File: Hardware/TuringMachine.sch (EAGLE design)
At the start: 91 parts, among them IC1 TL072P, IC11 78L09, IC12 78L09, IC5 4016, IC6 TL072P, IC7 TL072P, T1 2N3904

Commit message: add 100k resistor after noise comparator
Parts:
- removed IC5: 4016, 40xx:4016N
- added BACK_BUS: (no value), MusicThingModular:MA07-2_BACKSIDEFRONTSIDE
- added BACK_PWR: (no value), con-lstb:MA03-2
- added FRONT_BUS: (no value), MusicThingModular:MA07-2_BACKSIDEBACKSIDE
- added FRONT_PWR: (no value), MusicThingModular:MA03-2BACKSIDE
- added R4: 100k, TomW:R-EU_0207/7
- added SWITCH_IC: 4016, 40xx:4016N
- CLOCK, CV_IN, CV_OUT, NOISE-OUT: value THONKICONN -> THONKICONNNEW; device MusicThingModular:THONKICONN -> MusicThingModular:THONKICONNNEW
- R11: device MusicThingModular:RESISTOR6MM -> MusicThingModular:RESISTOR7MM
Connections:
- net NOISE renamed NOISE_FRONT
- removed net -12V: R35.1
- removed net B1: 1.A, LENGTH.6, R14.2, SHIFTREG_MAINA.QD, U$2.B1-MSB
- removed net B2: 2.A, SHIFTREG_MAINA.QC, U$2.B2
- removed net B3: 3.A, LENGTH.5, SHIFTREG_MAINA.QB, U$2.B3
- removed net B4: 4.A, LENGTH.4, SHIFTREG_MAINA.QA, U$2.B4
- removed net B5: 5.A, LENGTH.3, R8.1, SHIFTREG_MAINB.QD, U$2.B5
- removed net B6: 6.A, LENGTH.2, SHIFTREG_MAINB.QC, U$2.B6
- removed net B7: 7.A, LENGTH.1, SHIFTREG_MAINB.QB, U$2.B7
- removed net B8: 8.A, SHIFTREG_MAINB.QA, U$2.B8-LSB
- removed net BIT1_BACK: AND_2D.I0, BUFFER2F.I
- removed net BIT2_BACK: AND_2C.I1, BUFFER2E.I
- removed net BIT3_BACK: AND_2A.I0, BUFFER2A.I
- removed net BIT4_BACK: AND_2B.I0, BUFFER2B.I
- removed net BIT5_BACK: AND_1D.I0, BUFFER1E.I
- removed net BIT6_BACK: AND_1C.I0, BUFFER1D.I
- removed net BIT7_BACK: AND_1B.I0, BUFFER1C.I
- removed net BIT8_BACK: AND_1A.I0, BUFFER1A.I
- removed net CLOCKIN: CLK.A, D2.C, R12.2, R7.2, SHIFTREG_EXTA.CLK, SHIFTREG_EXTB.CLK, SHIFTREG_MAINA.CLK, SHIFTREG_MAINB.CLK
- removed net END_OF_LOOP: IC5A.A, IC5C.C, LENGTH.A
- removed net GND: C1.1, C2.2, C3.1, C4.1, CV_IN.5, IC5C.B, IC5D.B, IC6A.+IN, SHIFTREG_EXTA.RES, SHIFTREG_EXTB.RES, SHIFTREG_MAINA.RES, SHIFTREG_MAINB.RES, VR2.P$1, WRITE.S
- removed net N$24: IC5A.C, IC5D.C, IC6B.OUT
- removed net STEP_12: C3.2, LENGTH.7, R15.2, SHIFTREG_EXTA.D
- removed net STEP_16: LENGTH.8, SHIFTREG_EXTA.QD
- new net B1_BACK: AND_2D.I0, BACK_BUS.1, BUFFER2F.I, R14.2, SHIFTREG_MAINA.QD
- new net B1_FRONT: 1.A, FRONT_BUS.1, LENGTH.6, U$2.B1-MSB
- new net B2_BACK: AND_2C.I1, BACK_BUS.2, BUFFER2E.I, SHIFTREG_MAINA.QC
- new net B2_FRONT: 2.A, FRONT_BUS.2, U$2.B2
- new net B3_BACK: AND_2A.I0, BACK_BUS.3, BUFFER2A.I, SHIFTREG_MAINA.QB
- new net B3_FRONT: 3.A, FRONT_BUS.3, LENGTH.5, U$2.B3
- new net B4_BACK: AND_2B.I0, BACK_BUS.4, BUFFER2B.I, SHIFTREG_MAINA.QA
- new net B4_FRONT: 4.A, FRONT_BUS.4, LENGTH.4, U$2.B4
- new net B5_BACK: AND_1D.I0, BACK_BUS.5, BUFFER1E.I, R8.1, SHIFTREG_MAINB.QD
- new net B5_FRONT: 5.A, FRONT_BUS.5, LENGTH.3, U$2.B5
- new net B6_BACK: AND_1C.I0, BACK_BUS.6, BUFFER1D.I, SHIFTREG_MAINB.QC
- new net B6_FRONT: 6.A, FRONT_BUS.6, LENGTH.2, U$2.B6
- new net B7_BACK: AND_1B.I0, BACK_BUS.7, BUFFER1C.I, SHIFTREG_MAINB.QB
- new net B7_FRONT: 7.A, FRONT_BUS.7, LENGTH.1, U$2.B7
- new net B8_BACK: AND_1A.I0, BACK_BUS.8, BUFFER1A.I, SHIFTREG_MAINB.QA
- new net B8_FRONT: 8.A, FRONT_BUS.8, U$2.B8-LSB
- new net CLOCK_FRONT: CLK.A, D2.C, FRONT_BUS.11, R12.2, R7.2
- new net END_OF_LOOP_BACK: BACK_BUS.14, SWITCH_ICA.A, SWITCH_ICC.C
- new net END_OF_LOOP_FRONT: FRONT_BUS.14, LENGTH.A
- new net LOOP_CTRL_BACK: BACK_BUS.12, SWITCH_ICA.C, SWITCH_ICD.C
- new net LOOP_CTRL_FRONT: FRONT_BUS.12, R4.2
- new net N$1: IC6B.OUT, R4.1
- new net STEP_12_BACK: BACK_BUS.9, C3.2, R15.2, SHIFTREG_EXTA.D
- new net STEP_12_FRONT: FRONT_BUS.9, LENGTH.7
- new net STEP_16_BACK: BACK_BUS.10, SHIFTREG_EXTA.QD
- new net STEP_16_FRONT: FRONT_BUS.10, LENGTH.8
- new net WRITE_SW_FRONT: FRONT_BUS.13, R18.2
- net +12V_BACK: now also BACK_PWR.5, BACK_PWR.6, L1.2, R1.2, R24.2, SHIFTREG_EXTP.VDD, SHIFTREG_MAINP.VDD, SWITCH_ICP.VDD; no longer L1.1
- net +12V_FRONT: now also FRONT_PWR.5, FRONT_PWR.6; no longer IC5P.VDD, R1.2, R24.2, SHIFTREG_EXTP.VDD, SHIFTREG_MAINP.VDD
- net -12V_BACK: now also BACK_PWR.1, BACK_PWR.2, L2.2; no longer L2.1
- net -12V_FRONT: now also FRONT_PWR.1, FRONT_PWR.2, R35.1
- net CLOCK_BACK: now also BACK_BUS.11, SHIFTREG_EXTA.CLK, SHIFTREG_EXTB.CLK, SHIFTREG_MAINA.CLK, SHIFTREG_MAINB.CLK
- net GND_BACK: now also BACK_PWR.3, BACK_PWR.4, C1.1, C2.2, C3.1, C4.1, SHIFTREG_EXTA.RES, SHIFTREG_EXTB.RES, SHIFTREG_EXTP.VSS, SHIFTREG_MAINA.RES, SHIFTREG_MAINB.RES, SHIFTREG_MAINP.VSS, SWITCH_ICC.B, SWITCH_ICD.B, SWITCH_ICP.VSS
- net GND_FRONT: now also CV_IN.5, FRONT_PWR.3, FRONT_PWR.4, IC6A.+IN, VR2.P$1, WRITE.S; no longer IC5P.VSS, SHIFTREG_EXTP.VSS, SHIFTREG_MAINP.VSS
- net N$4: now also SWITCH_ICB.A, SWITCH_ICC.A; no longer IC5B.A, IC5C.A
- net N$42: now also L1.1; no longer L1.2
- net N$44: now also L2.1; no longer L2.2
- net N$45: now also SWITCH_ICB.C, SWITCH_ICD.A; no longer IC5B.C, IC5D.A
- net START_OF_LOOP: now also BACK_BUS.13, SWITCH_ICA.B, SWITCH_ICB.B; no longer IC5A.B, IC5B.B, R18.2
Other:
- note added: "Channels between front and back: GND +12V -12V STEP_16_FRONT - STEP_16_BACK STEP_12_FRONT - STEP_12_BACK CLOCK_FRONT - CLOCK_BACK END_OF_LOOP_FRONT - END_OF_LOOP_BACKRL LOOP_CTRL_FRONT - LOOP_CTRL_BACK WRITE_SW_FRONT - START_OF_LOOP B1(-B8)_FRONT - B1(-B8)_BACK"
- moved on the sheet: AND_1A, AND_1B, AND_1C, AND_1D, AND_2A, AND_2B, AND_2C, AND_2D, BUFFER1A, BUFFER1B, BUFFER1C, BUFFER1D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

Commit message: routing
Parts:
- removed IC1, IC6: TL072P, TomW:TL072P
- added U1: TL074_, MusicThingModular:TL074_
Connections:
- net N$29 renamed +9V_1
- net N$38 renamed +9V_2
- new net N$17: R16.2, SWITCH_ICA.B, SWITCH_ICB.B
- net +12V_FRONT: now also R29.2, U1P.V+; no longer IC1P.V+, IC6P.V+, R29.1
- net -12V_FRONT: now also U1P.V-; no longer IC1P.V-, IC6P.V-
- net B1_BACK: now also AND_2C.I0, BUFFER2D.I, R14.1; no longer AND_2D.I0, BUFFER2F.I, R14.2
- net B2_BACK: now also AND_2D.I1; no longer AND_2C.I1
- net B3_BACK: now also AND_2B.I0, BUFFER2C.I; no longer AND_2A.I0, BUFFER2A.I
- net B4_BACK: now also AND_2A.I0; no longer AND_2B.I0
- net B8_BACK: now also BUFFER1B.I; no longer BUFFER1A.I
- net BUFFCLK2_BACK: now also BUFFER1A.O; no longer BUFFER2D.O
- net BUFFCLK_BACK: now also AND_2C.I1, AND_2D.I0, BUFFER2A.O; no longer AND_2C.I0, AND_2D.I1, BUFFER2C.O
- net CLOCK_BACK: now also BUFFER1A.I, BUFFER2A.I; no longer BUFFER2C.I, BUFFER2D.I
- net CLOCK_FRONT: now also R13.2; no longer CLK.A
- net GATE1: now also BUFFER2D.O; no longer BUFFER2F.O
- net GATE3: now also BUFFER2C.O; no longer BUFFER2A.O
- net GATE8: now also BUFFER1B.O; no longer BUFFER1A.O
- net GND_BACK: now also BUFFER2F.I, C2.1; no longer BUFFER1B.I, C2.2
- net GND_FRONT: now also CLK.C, U1A.+IN, U1B.+IN, U1C.+IN; no longer IC1A.+IN, IC1B.+IN, IC6A.+IN, R13.1
- net N$1: now also U1D.OUT; no longer IC6B.OUT
- net N$15: now also CLK.A, R13.1; no longer CLK.C, R13.2
- net N$16: now also R29.1; no longer R29.2
- net N$21: now also U1A.-IN; no longer IC1A.-IN
- net N$22: now also U1A.OUT; no longer IC1A.OUT
- net N$27: now also U1B.-IN; no longer IC1B.-IN
- net N$28: now also C2.2, R14.2; no longer C2.1, R14.1
- net N$41: now also U1B.OUT; no longer IC1B.OUT
- net N$6: now also U1C.-IN; no longer IC6A.-IN
- net N$7: now also U1C.OUT, U1D.-IN; no longer IC6A.OUT, IC6B.-IN
- net NOISE_FRONT: now also U1D.+IN; no longer IC6B.+IN
- net PULSE1: now also AND_2C.O; no longer AND_2D.O
- net PULSE2: now also AND_2D.O; no longer AND_2C.O
- net PULSE3: now also AND_2B.O; no longer AND_2A.O
- net PULSE4: now also AND_2A.O; no longer AND_2B.O
- net START_OF_LOOP: no longer R16.2, SWITCH_ICA.B, SWITCH_ICB.B
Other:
- moved on the sheet: AND_2A, AND_2B, AND_2C, AND_2D, BUFFER1A, BUFFER1B, BUFFER2A, BUFFER2C, BUFFER2D, BUFFER2F, C2, C4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

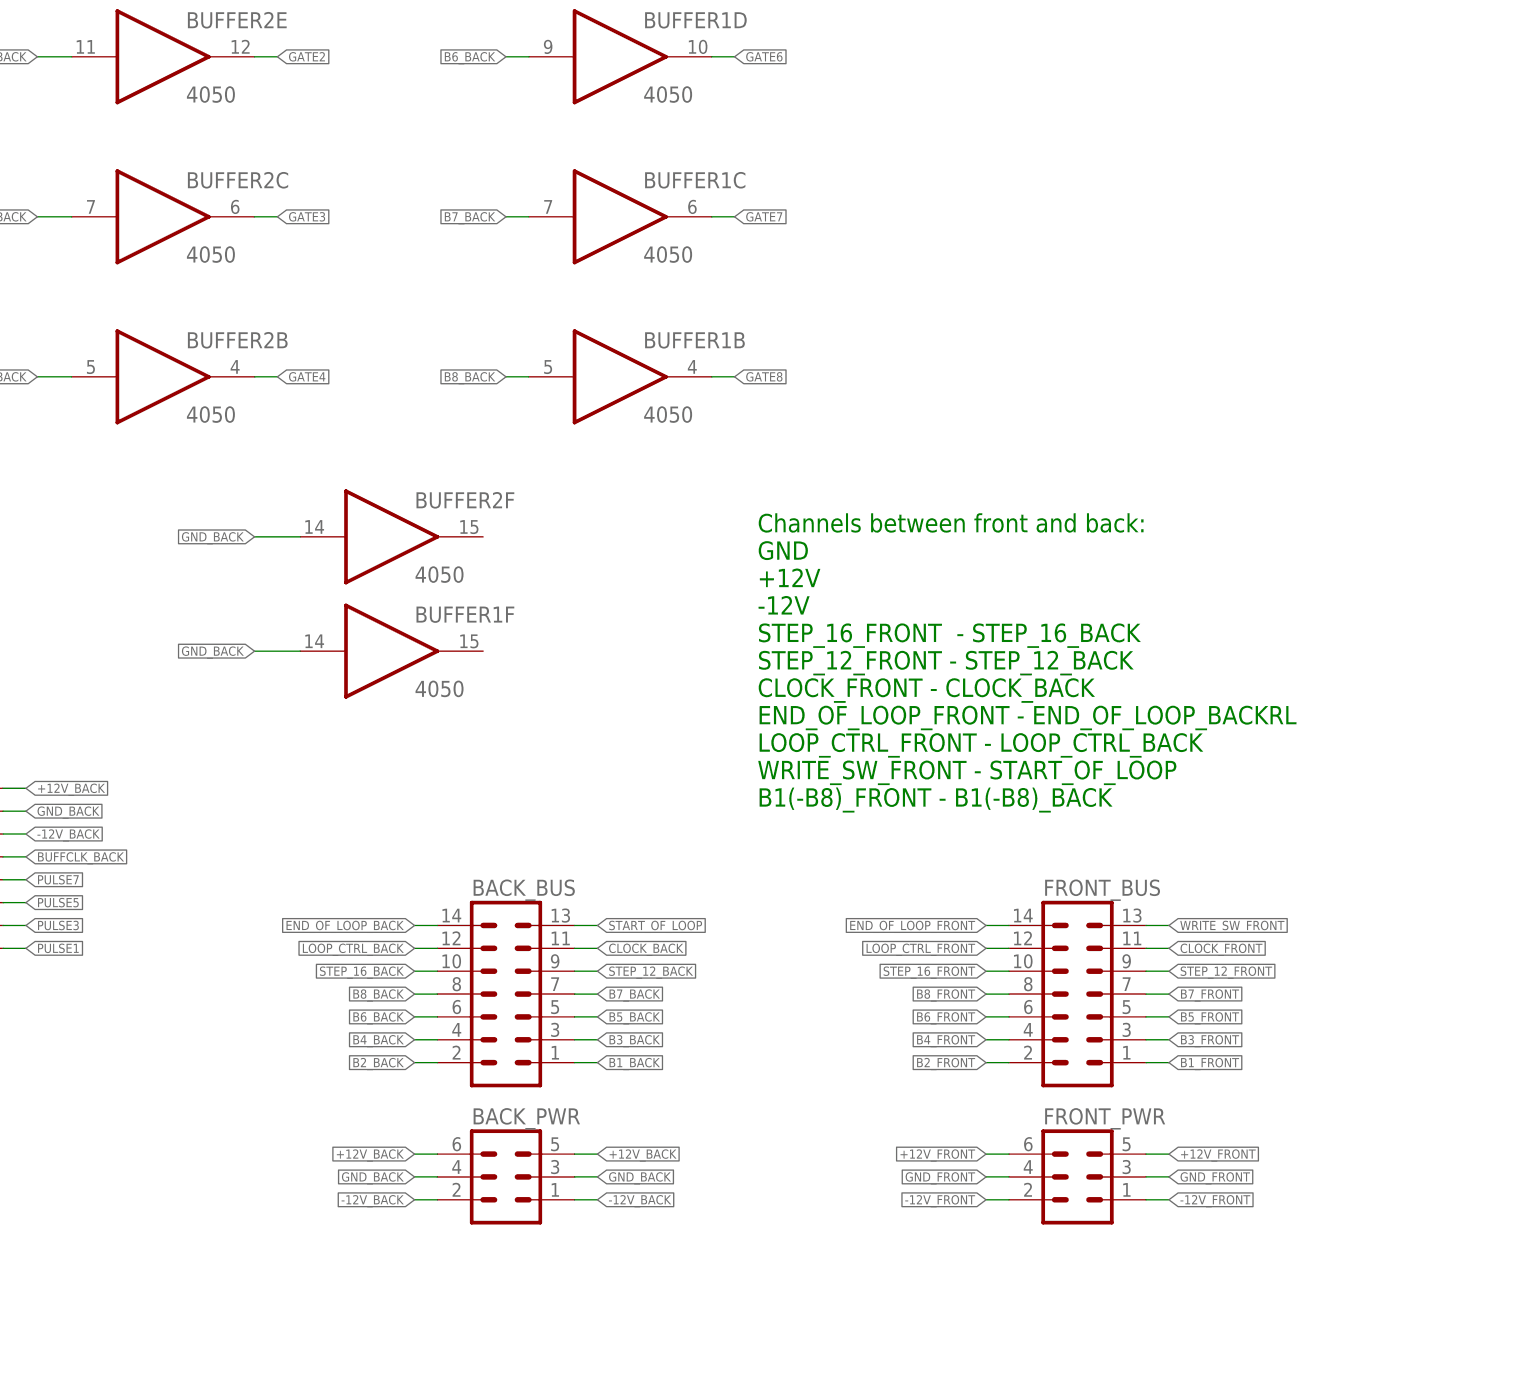
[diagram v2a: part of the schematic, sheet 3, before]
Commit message: Adding pulse out
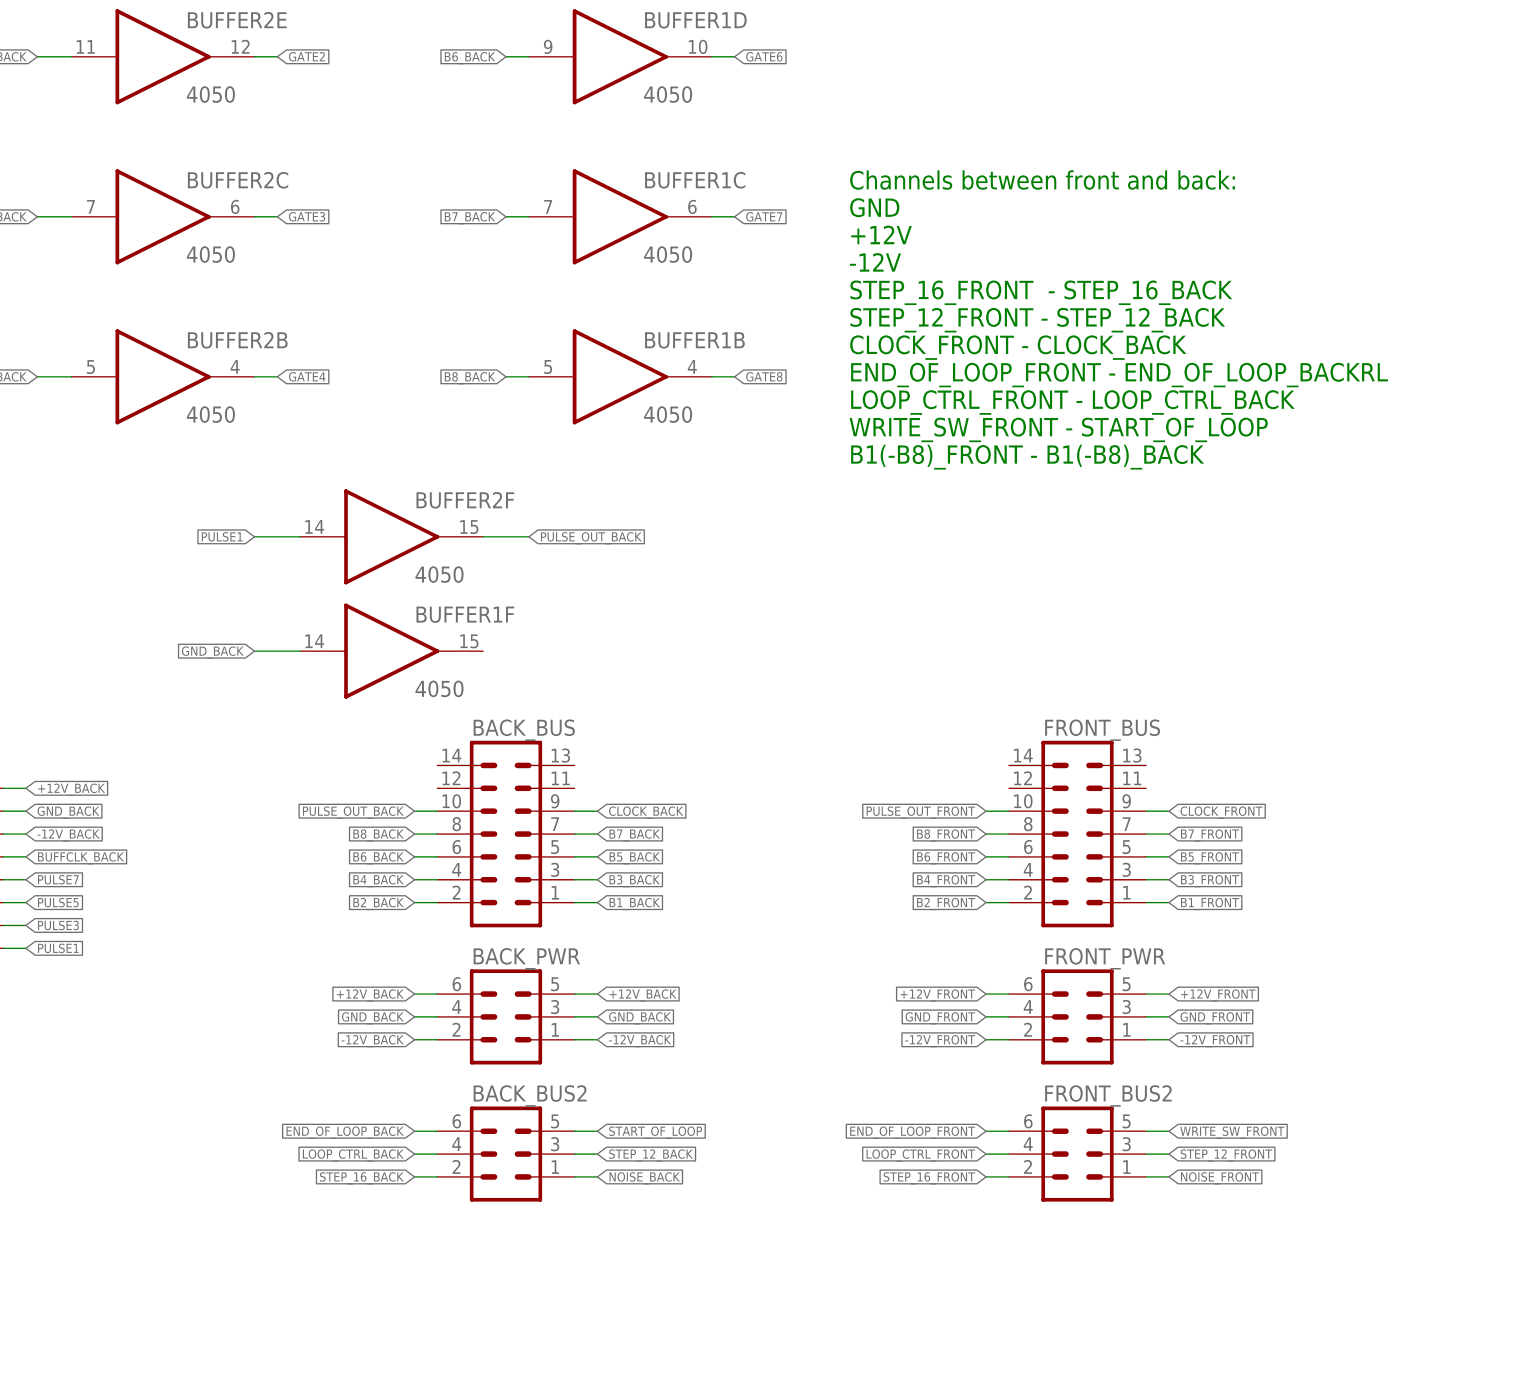
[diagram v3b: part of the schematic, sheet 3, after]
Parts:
- added BACK_BUS2: (no value), con-lstb:MA03-2
- added C19, C20, C21, C22, C23, C24, C25: 100n, TomW:C-EU050-024X044
- added FRONT_BUS2: (no value), MusicThingModular:MA03-2BACKSIDE
- added PULS1: (no value), TomW:LED3MM
- added PULSE_OUT: THONKICONNNEW, MusicThingModular:THONKICONNNEW
- added R17: 2.2k, TomW:R-EU_0207/7
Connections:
- new net NOISE_BACK: BACK_BUS2.1, IC7B.+IN
- new net PULSE_OUT_BACK: BACK_BUS.10, BUFFER2F.O
- new net PULSE_OUT_FRONT: FRONT_BUS.10, PULSE_OUT.3, R17.2
- net +12V_BACK: now also C19.1, C20.1, C21.1, C22.1, C23.1, IC7P.V+
- net +12V_FRONT: no longer IC7P.V+
- net +9V_1: now also C24.2
- net +9V_2: now also C25.2
- net -12V_BACK: now also IC7P.V-
- net -12V_FRONT: no longer IC7P.V-
- net CLOCK_BACK: now also BACK_BUS.9; no longer BACK_BUS.11
- net CLOCK_FRONT: now also FRONT_BUS.9; no longer FRONT_BUS.11
- net END_OF_LOOP_BACK: now also BACK_BUS2.6; no longer BACK_BUS.14
- net END_OF_LOOP_FRONT: now also FRONT_BUS2.6; no longer FRONT_BUS.14
- net GND_BACK: now also C19.2, C20.2, C21.2, C22.2, C23.2, C24.1, C25.1, IC7A.+IN; no longer BUFFER2F.I
- net GND_FRONT: now also PULS1.C, PULSE_OUT.5; no longer IC7A.+IN
- net LOOP_CTRL_BACK: now also BACK_BUS2.4, IC7A.-IN, R4.2, R6.2; no longer BACK_BUS.12
- net LOOP_CTRL_FRONT: now also FRONT_BUS2.4, R22.1, R5.2; no longer FRONT_BUS.12, R4.2
- net MAIN_OUT: now also U1C.OUT; no longer IC7A.OUT
- net N$1: now also IC7B.OUT; no longer U1D.OUT
- net N$12: now also U1D.-IN; no longer IC7B.-IN
- net N$13: now also U1C.-IN; no longer IC7A.-IN
- net N$5: now also U1D.+IN; no longer IC7B.+IN
- net N$6: now also PULS1.A, R17.1; no longer R22.1, R5.2, R6.2, U1C.-IN
- net N$7: now also IC7A.OUT, IC7B.-IN; no longer U1C.OUT, U1D.-IN
- net N$8: now also U1D.OUT; no longer IC7B.OUT
- net NOISE_FRONT: now also FRONT_BUS2.1; no longer U1D.+IN
- net PULSE1: now also BUFFER2F.I
- net START_OF_LOOP: now also BACK_BUS2.5; no longer BACK_BUS.13
- net STEP_12_BACK: now also BACK_BUS2.3; no longer BACK_BUS.9
- net STEP_12_FRONT: now also FRONT_BUS2.3; no longer FRONT_BUS.9
- net STEP_16_BACK: now also BACK_BUS2.2; no longer BACK_BUS.10
- net STEP_16_FRONT: now also FRONT_BUS2.2; no longer FRONT_BUS.10
- net WRITE_SW_FRONT: now also FRONT_BUS2.5; no longer FRONT_BUS.13
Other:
- moved on the sheet: BACK_BUS, BACK_PWR, CV_IN, FRONT_BUS, FRONT_PWR, R22, R23, R35, R5, VR2

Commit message: Before board split
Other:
- moved on the sheet: R29
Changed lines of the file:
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@@
 <instance part="C13" gate="G$1" x="88.9" y="200.66"/>
 <instance part="T1" gate="G1" x="144.78" y="71.12" rot="R180"/>
-<instance part="R29" gate="G$1" x="142.24" y="83.82" rot="R270"/>
+<instance part="R29" gate="G$1" x="142.24" y="83.82" rot="R90"/>
 <instance part="C10" gate="G$1" x="152.4" y="78.74" rot="R90"/>
 <instance part="R30" gate="G$1" x="162.56" y="78.74"/>
@@
 <segment>
 <pinref part="R29" gate="G$1" pin="2"/>
-<wire x1="142.24" y1="91.44" x2="142.24" y2="78.74" width="0.1524" layer="91"/>
+<wire x1="142.24" y1="91.44" x2="142.24" y2="88.9" width="0.1524" layer="91"/>
 <label x="142.24" y="90.17" size="1.016" layer="95" rot="R90" xref="yes"/>
 </segment>
@@
 <pinref part="T1" gate="G1" pin="E"/>
 <pinref part="R29" gate="G$1" pin="1"/>
-<wire x1="142.24" y1="76.2" x2="142.24" y2="88.9" width="0.1524" layer="91"/>
+<wire x1="142.24" y1="76.2" x2="142.24" y2="78.74" width="0.1524" layer="91"/>
 <pinref part="C10" gate="G$1" pin="1"/>
-<wire x1="149.86" y1="78.74" x2="142.24" y2="88.9" width="0.1524" layer="91"/>
-<junction x="142.24" y="88.9"/>
-</segment>
-</net>
+<wire x1="149.86" y1="78.74" x2="142.24" y2="78.74" width="0.1524" layer="91"/>
+<junction x="142.24" y="78.74"/>
+</segment>
+</net>
